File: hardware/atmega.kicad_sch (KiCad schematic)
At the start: 12 parts, among them J3 ICSP, SW1 SW_SPST, U101 ATmega328-A, Y1 Crystal_GND2

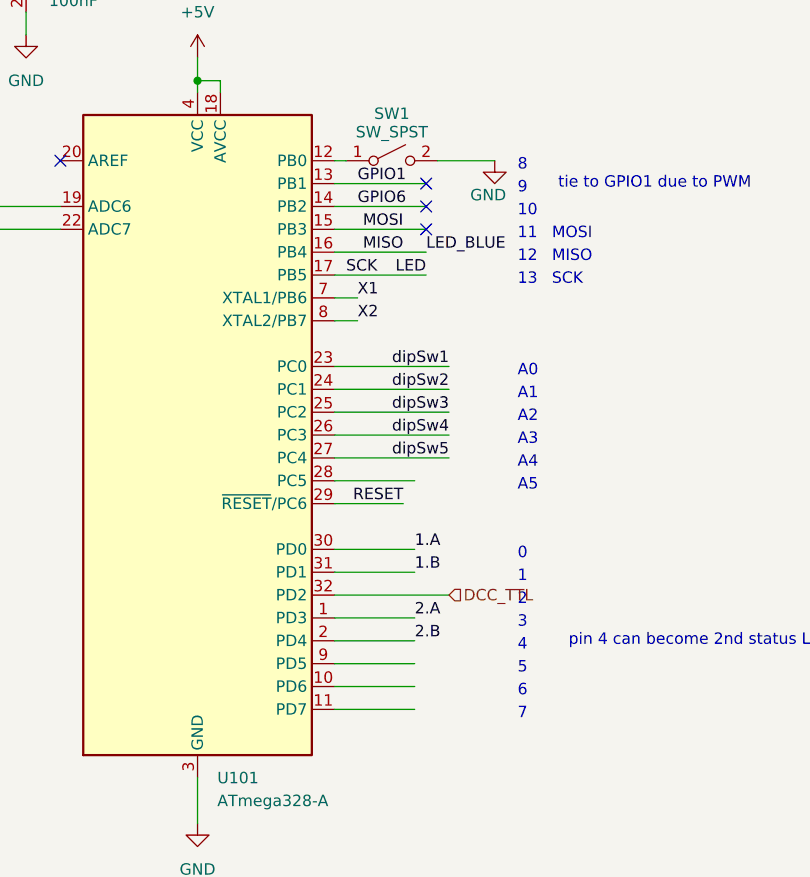
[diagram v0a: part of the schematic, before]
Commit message: changed LDO
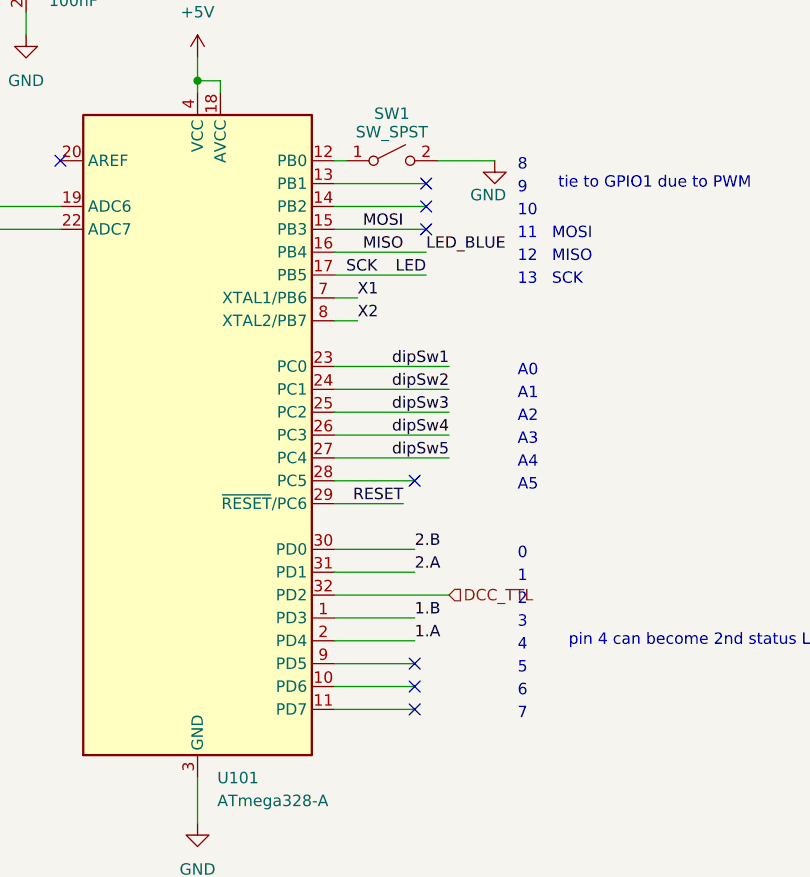
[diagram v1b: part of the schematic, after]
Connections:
- net 1.A: now also U101.2 (PD4); no longer U101.30 (PD0)
- net 1.B: now also U101.1 (PD3); no longer U101.31 (PD1)
- net 2.A: now also U101.31 (PD1); no longer U101.1 (PD3)
- net 2.B: now also U101.30 (PD0); no longer U101.2 (PD4)
- net GPIO1: no longer names the net of U101.13 (PB1)
- net GPIO6: no longer names the net of U101.14 (PB2)
- no-connect marks 6 -> 10
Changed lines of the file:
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@@
+	)
+	(no_connect
+		(at 158.75 143.51)
 	)
 	(no_connect
@@
 	)
 	(no_connect
+		(at 158.75 118.11)
+	)
+	(no_connect
 		(at 160.02 90.17)
 	)
@@
 	(no_connect
 		(at 110.49 90.17)
+	)
+	(no_connect
+		(at 158.75 138.43)
+	)
+	(no_connect
+		(at 158.75 140.97)
 	)
 	(bus_entry
@@
 		)
 	)
-	(label "GPIO1"
-		(at 152.4 85.09 0)
-		(effects
-			(font
-				(size 1.27 1.27)
-			)
-			(justify left bottom)
-		)
-	)
 	(label "MISO"
 		(at 93.98 146.05 180)
@@
 	)
 	(label "2.B"
-		(at 158.75 135.89 0)
+		(at 158.75 125.73 0)
 		(effects
 			(font
@@
 		)
 	)
-	(label "GPIO6"
-		(at 152.4 87.63 0)
-		(effects
-			(font
-				(size 1.27 1.27)
-			)
-			(justify left bottom)
-		)
-	)
 	(label "1.B"
 		(at 218.44 96.52 0)
@@
 	)
 	(label "2.A"
-		(at 158.75 133.35 0)
+		(at 158.75 128.27 0)
 		(effects
 			(font
@@
 	)
 	(label "1.B"
-		(at 158.75 128.27 0)
+		(at 158.75 133.35 0)
 		(effects
 			(font
@@
 	)
 	(label "1.A"
-		(at 158.75 125.73 0)
-		(effects
-			(font
+		(at 158.75 135.89 0)
+		(effects
+			(font
